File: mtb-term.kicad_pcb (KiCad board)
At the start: 2 copper layers, 22 x 14.5 mm, 10 parts, among them J1 Conn_01x04, U1 L78L05_SOT89

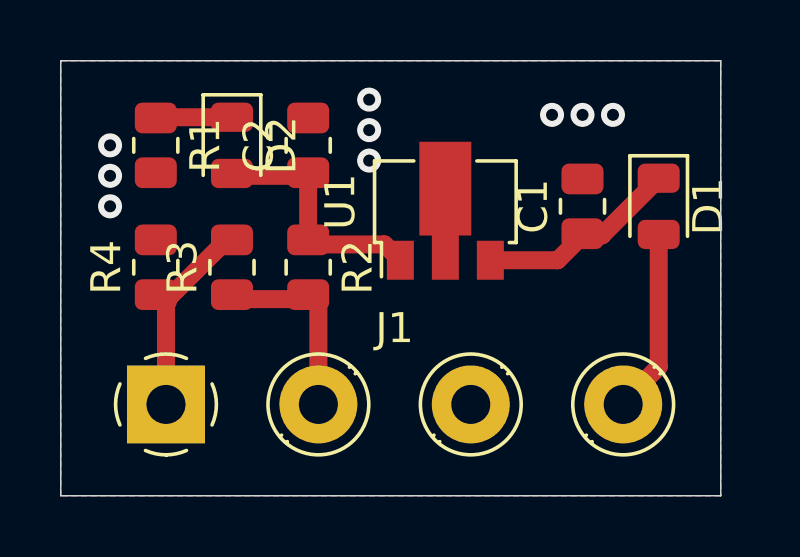
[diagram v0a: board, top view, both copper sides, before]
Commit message: Add pins description to silkscreen.
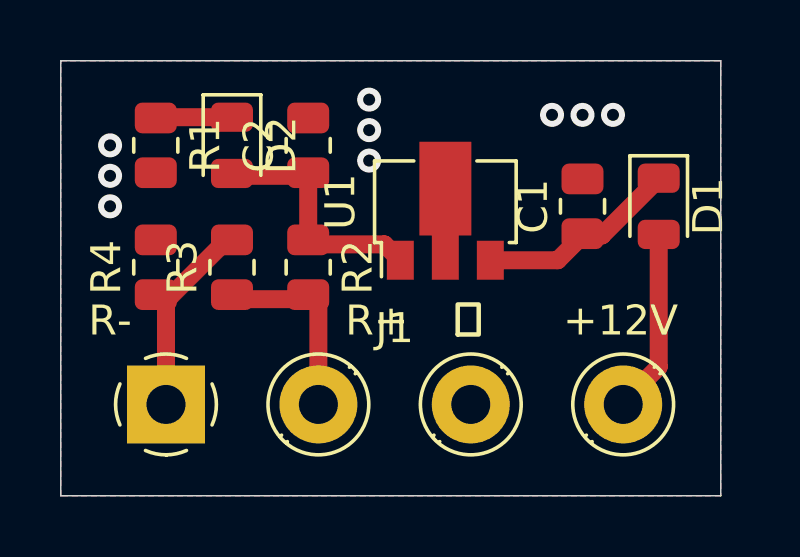
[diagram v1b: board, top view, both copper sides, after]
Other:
- board text added: "+12V"
- board text added: "R+"
- board text added: "R-"
- board text added: "⏚"
